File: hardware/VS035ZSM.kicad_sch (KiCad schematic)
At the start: 41 parts, among them IC3 TPS65131TRGERQ1, J2 FH35C-25S-0.3SHW_50_, J4 245863050104829+, U4 LP3320

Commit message: updated tps6513 footprint to vqfn24 + fixed some missing connections near it
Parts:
- IC3: footprint SamacSys_Parts:QFN50P400X400X100-25N-D -> Package_DFN_QFN:VQFN-24-1EP_4x4mm_P0.5mm_EP2.45x2.45mm
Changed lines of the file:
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@@
       (effects (font (size 1.27 1.27)))
     )
-    (property "Footprint" "SamacSys_Parts:QFN50P400X400X100-25N-D" (at 167.64 142.545 0)
+    (property "Footprint" "Package_DFN_QFN:VQFN-24-1EP_4x4mm_P0.5mm_EP2.45x2.45mm" (at 167.64 142.545 0)
       (effects (font (size 1.27 1.27)) (justify left top) hide)
     )

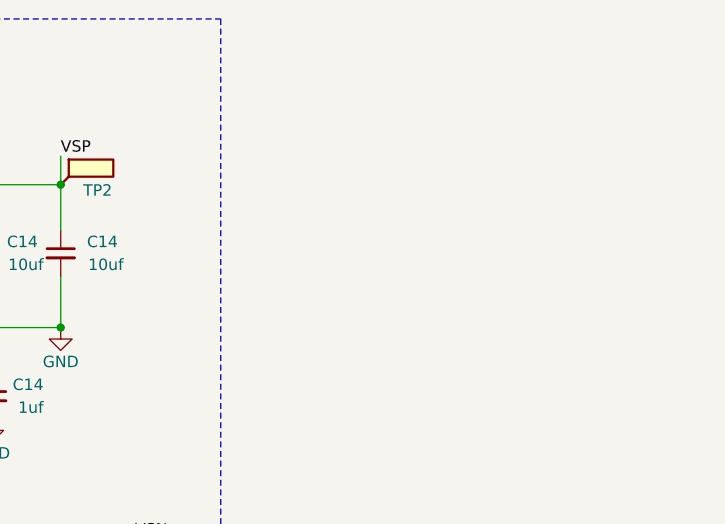
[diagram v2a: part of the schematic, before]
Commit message: added via stitching and updated the bias generator layout
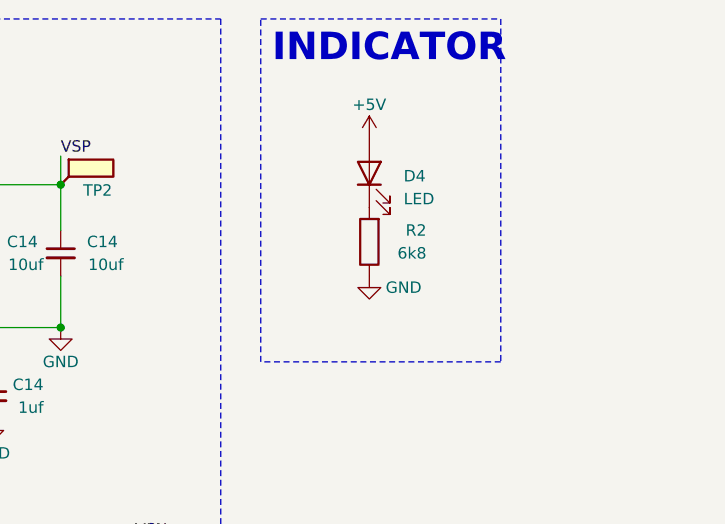
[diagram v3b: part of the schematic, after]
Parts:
- added D4: LED, LED_SMD:LED_0805_2012Metric, symbol Device:LED
- added R2: 6k8, Resistor_SMD:R_0603_1608Metric, symbol Device:R
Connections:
- net +5V: now also D4.2 (A)
- net GND: now also R2.1
- new net: D4.1 (K), R2.2
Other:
- note added: "INDICATOR"
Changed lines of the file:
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@@
+    (fill (type none))
+  )
+  (rectangle (start 227.33 14.605) (end 254 52.705)
+    (stroke (width 0) (type dash))
     (fill (type none))
   )
@@
     (effects (font (face "KiCad Font") (size 3.048 3.048) (thickness 0.3556) bold) (justify left bottom))
   )
+  (text "INDICATOR" (at 228.6 19.685 0)
+    (effects (font (face "KiCad Font") (size 3.048 3.048) (thickness 0.3556) bold) (justify left bottom))
+  )
   (text "DISP MEZZANINE" (at 17.145 93.345 0)
     (effects (font (face "KiCad Font") (size 3.048 3.048) (thickness 0.3556) bold) (justify left bottom))
@@
         (path "/e63e39d7-6ac0-4ffd-8aa3-1841a4541b55/aa1c650f-a854-42b3-a05e-cf0d26468eda"
           (reference "#PWR041") (unit 1)
+        )
+      )
+    )
+  )
+  (symbol (lib_id "Device:R") (at 239.395 39.37 180) (unit 1)
+    (in_bom yes) (on_board yes) (dnp no)
+    (property "Reference" "R2" (at 245.745 38.1 0)
+      (effects (font (size 1.27 1.27)) (justify left))
+    )
+    (property "Value" "6k8" (at 245.745 40.64 0)
+      (effects (font (size 1.27 1.27)) (justify left))
+    )
+    (property "Footprint" "Resistor_SMD:R_0603_1608Metric" (at 241.173 39.37 90)
+      (effects (font (size 1.27 1.27)) hide)
+    )
+    (property "Datasheet" "~" (at 239.395 39.37 0)
+      (effects (font (size 1.27 1.27)) hide)
+    )
+    (pin "1")
+    (pin "2")
+    (instances
+      (project "ssd2828_board"
+        (path "/e63e39d7-6ac0-4ffd-8aa3-1841a4541b55"
+          (reference "R2") (unit 1)
+        )
+        (path "/e63e39d7-6ac0-4ffd-8aa3-1841a4541b55/eadf4466-e824-4ab1-a46a-9025d68137a1"
+          (reference "R11") (unit 1)
+        )
+        (path "/e63e39d7-6ac0-4ffd-8aa3-1841a4541b55/d0befddb-c525-47aa-a36b-f999bfb6acb2"
+          (reference "R14") (unit 1)
+        )
+        (path "/e63e39d7-6ac0-4ffd-8aa3-1841a4541b55/aa1c650f-a854-42b3-a05e-cf0d26468eda"
+          (reference "R14") (unit 1)
         )
       )
@@
         (path "/e63e39d7-6ac0-4ffd-8aa3-1841a4541b55/aa1c650f-a854-42b3-a05e-cf0d26468eda"
           (reference "#PWR081") (unit 1)
+        )
+      )
+    )
+  )
+  (symbol (lib_name "GND_3") (lib_id "power:GND") (at 239.395 43.18 0) (unit 1)
+    (in_bom yes) (on_board yes) (dnp no)
+    (property "Reference" "#PWR03" (at 239.395 49.53 0)
+      (effects (font (size 1.27 1.27)) hide)
+    )
+    (property "Value" "GND" (at 243.205 44.45 0)
+      (effects (font (size 1.27 1.27)))
+    )
+    (property "Footprint" "" (at 239.395 43.18 0)
+      (effects (font (size 1.27 1.27)) hide)
+    )
+    (property "Datasheet" "" (at 239.395 43.18 0)
+      (effects (font (size 1.27 1.27)) hide)
+    )
+    (pin "1")
+    (instances
+      (project "ssd2828_board"
+        (path "/e63e39d7-6ac0-4ffd-8aa3-1841a4541b55"
+          (reference "#PWR03") (unit 1)
+        )
+        (path "/e63e39d7-6ac0-4ffd-8aa3-1841a4541b55/eadf4466-e824-4ab1-a46a-9025d68137a1"
+          (reference "#PWR099") (unit 1)
+        )
+        (path "/e63e39d7-6ac0-4ffd-8aa3-1841a4541b55/aa1c650f-a854-42b3-a05e-cf0d26468eda"
+          (reference "#PWR0101") (unit 1)
         )
       )
@@
     )
   )
+  (symbol (lib_id "Device:LED") (at 239.395 31.75 90) (unit 1)
+    (in_bom yes) (on_board yes) (dnp no) (fields_autoplaced)
+    (property "Reference" "D4" (at 243.205 32.0675 90)
+      (effects (font (size 1.27 1.27)) (justify right))
+    )
+    (property "Value" "LED" (at 243.205 34.6075 90)
+      (effects (font (size 1.27 1.27)) (justify right))
+    )
+    (property "Footprint" "LED_SMD:LED_0805_2012Metric" (at 239.395 31.75 0)
+      (effects (font (size 1.27 1.27)) hide)
+    )
+    (property "Datasheet" "~" (at 239.395 31.75 0)
+      (effects (font (size 1.27 1.27)) hide)
+    )
+    (pin "1")
+    (pin "2")
+    (instances
+      (project "ssd2828_board"
+        (path "/e63e39d7-6ac0-4ffd-8aa3-1841a4541b55/eadf4466-e824-4ab1-a46a-9025d68137a1"
+          (reference "D4") (unit 1)
+        )
+        (path "/e63e39d7-6ac0-4ffd-8aa3-1841a4541b55/aa1c650f-a854-42b3-a05e-cf0d26468eda"
+          (reference "D5") (unit 1)
+        )
+      )
+    )
+  )
   (symbol (lib_id "Device:C_Small") (at 205.105 40.64 0) (mirror y) (unit 1)
     (in_bom yes) (on_board yes) (dnp no)
@@
         )
       )
+    )
+  )
+  (symbol (lib_id "power:+5V") (at 239.395 27.94 0) (unit 1)
+    (in_bom yes) (on_board yes) (dnp no) (fields_autoplaced)
+    (property "Reference" "#PWR021" (at 239.395 31.75 0)
+      (effects (font (size 1.27 1.27)) hide)
+    )
+    (property "Value" "+5V" (at 239.395 24.13 0)
+      (effects (font (size 1.27 1.27)))
+    )
+    (property "Footprint" "" (at 239.395 27.94 0)
+      (effects (font (size 1.27 1.27)) hide)
+    )
+    (property "Datasheet" "" (at 239.395 27.94 0)
+      (effects (font (size 1.27 1.27)) hide)
+    )
+    (pin "1")
+    (instances
+      (project "ssd2828_board"
+        (path "/e63e39d7-6ac0-4ffd-8aa3-1841a4541b55/eadf4466-e824-4ab1-a46a-9025d68137a1"
+          (reference "#PWR021") (unit 1)
+        )
+        (path "/e63e39d7-6ac0-4ffd-8aa3-1841a4541b55/aa1c650f-a854-42b3-a05e-cf0d26468eda"
+          (reference "#PWR0100") (unit 1)
+        )
+      )

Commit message: fixed details
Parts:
- L5, L6: footprint Inductor_SMD:WPN252012 -> C98354:IND-SMD_L2.5-W2.0_WPN252012H
- L7: footprint Inductor_SMD:FHD252012 -> C602016:IND-SMD_L2.5-W2.0_FHD252012S-6R8MT
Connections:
- no-connect marks 0 -> 13
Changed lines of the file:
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@@
   (junction (at 27.94 140.335) (diameter 0) (color 0 0 0 0)
   )
+  (no_connect (at 67.945 112.395))
+  (no_connect (at 255.27 136.525))
+  (no_connect (at 67.945 120.015))
+  (no_connect (at 67.945 107.315))
+  (no_connect (at 67.945 125.095))
+  (no_connect (at 67.945 104.775))
+  (no_connect (at 252.73 136.525))
+  (no_connect (at 42.545 165.735))
+  (no_connect (at 67.945 122.555))
+  (no_connect (at 67.945 127.635))
+  (no_connect (at 250.19 136.525))
+  (no_connect (at 67.945 109.855))
+  (no_connect (at 42.545 160.655))
   (wire (pts (xy 83.185 130.175) (xy 83.185 132.715))
     (stroke (width 0) (type default))
@@
       (effects (font (size 1.27 1.27)))
     )
-    (property "Footprint" "Inductor_SMD:FHD252012" (at 135.89 123.19 0)
+    (property "Footprint" "C602016:IND-SMD_L2.5-W2.0_FHD252012S-6R8MT" (at 135.89 123.19 0)
       (effects (font (size 1.27 1.27)) hide)
     )
@@
       (effects (font (size 1.27 1.27)))
     )
-    (property "Footprint" "Inductor_SMD:WPN252012" (at 178.435 86.36 0)
+    (property "Footprint" "C98354:IND-SMD_L2.5-W2.0_WPN252012H" (at 178.435 86.36 0)
       (effects (font (size 1.27 1.27)) hide)
     )
@@
       (effects (font (size 1.27 1.27)))
     )
-    (property "Footprint" "Inductor_SMD:WPN252012" (at 132.08 33.02 0)
-      (effects (font (size 1.27 1.27)) hide)
-    )
+    (property "Footprint" "C98354:IND-SMD_L2.5-W2.0_WPN252012H" (at 132.08 33.02 0)
+      (effects (font (size 1.27 1.27)) hide)
+    )

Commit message: fixed some 3d models + redid power distribution on the BOE board
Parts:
- R2: footprint Resistor_SMD:R_0603_1608Metric -> Resistor_SMD:R_1210_3225Metric
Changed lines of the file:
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@@
       (effects (font (size 1.27 1.27)) (justify left))
     )
-    (property "Footprint" "Resistor_SMD:R_0603_1608Metric" (at 167.132 142.24 90)
+    (property "Footprint" "Resistor_SMD:R_1210_3225Metric" (at 167.132 142.24 90)
       (effects (font (size 1.27 1.27)) hide)
     )

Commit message: version 1.0
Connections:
- net +1V8: now also RN1.1 (R1.1)
- net GND: no longer RN1.1 (R1.1)
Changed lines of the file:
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@@
   (junction (at 195.58 90.17) (diameter 0) (color 0 0 0 0)
-  )
-  (junction (at 227.33 146.05) (diameter 0) (color 0 0 0 0)
   )
   (junction (at 178.435 90.17) (diameter 0) (color 0 0 0 0)
@@
     (stroke (width 0) (type default))
   )
+  (wire (pts (xy 220.345 147.955) (xy 224.79 147.955))
+    (stroke (width 0) (type default))
+  )
   (wire (pts (xy 178.435 76.2) (xy 178.435 71.755))
     (stroke (width 0) (type default))
@@
     (stroke (width 0) (type default))
   )
-  (wire (pts (xy 224.79 146.05) (xy 227.33 146.05))
-    (stroke (width 0) (type default))
-  )
   (wire (pts (xy 27.94 170.815) (xy 27.94 173.355))
     (stroke (width 0) (type default))
@@
     (stroke (width 0) (type default))
   )
+  (wire (pts (xy 224.79 147.955) (xy 224.79 146.05))
+    (stroke (width 0) (type default))
+  )
   (wire (pts (xy 34.925 107.315) (xy 42.545 107.315))
     (stroke (width 0) (type default))
@@
   )
   (wire (pts (xy 33.655 53.34) (xy 48.895 53.34))
+    (stroke (width 0) (type default))
+  )
+  (wire (pts (xy 220.345 146.05) (xy 220.345 147.955))
     (stroke (width 0) (type default))
   )
@@
         )
       )
+    )
+  )
+  (symbol (lib_id "power:+1V8") (at 220.345 146.05 0) (unit 1)
+    (in_bom yes) (on_board yes) (dnp no)
+    (property "Reference" "#PWR036" (at 220.345 149.86 0)
+      (effects (font (size 1.27 1.27)) hide)
+    )
+    (property "Value" "+1V8" (at 220.345 142.24 0)
+      (effects (font (size 1.27 1.27)))
+    )
+    (property "Footprint" "" (at 220.345 146.05 0)
+      (effects (font (size 1.27 1.27)) hide)
+    )
+    (property "Datasheet" "" (at 220.345 146.05 0)
+      (effects (font (size 1.27 1.27)) hide)
+    )
+    (pin "1")
+    (instances
+      (project "ssd2828_board"
+        (path "/e63e39d7-6ac0-4ffd-8aa3-1841a4541b55/eadf4466-e824-4ab1-a46a-9025d68137a1"
+          (reference "#PWR036") (unit 1)
+        )
+        (path "/e63e39d7-6ac0-4ffd-8aa3-1841a4541b55/d0befddb-c525-47aa-a36b-f999bfb6acb2"
+          (reference "#PWR046") (unit 1)
+        )
+        (path "/e63e39d7-6ac0-4ffd-8aa3-1841a4541b55/aa1c650f-a854-42b3-a05e-cf0d26468eda"
+          (reference "#PWR0105") (unit 1)
+        )
+      )

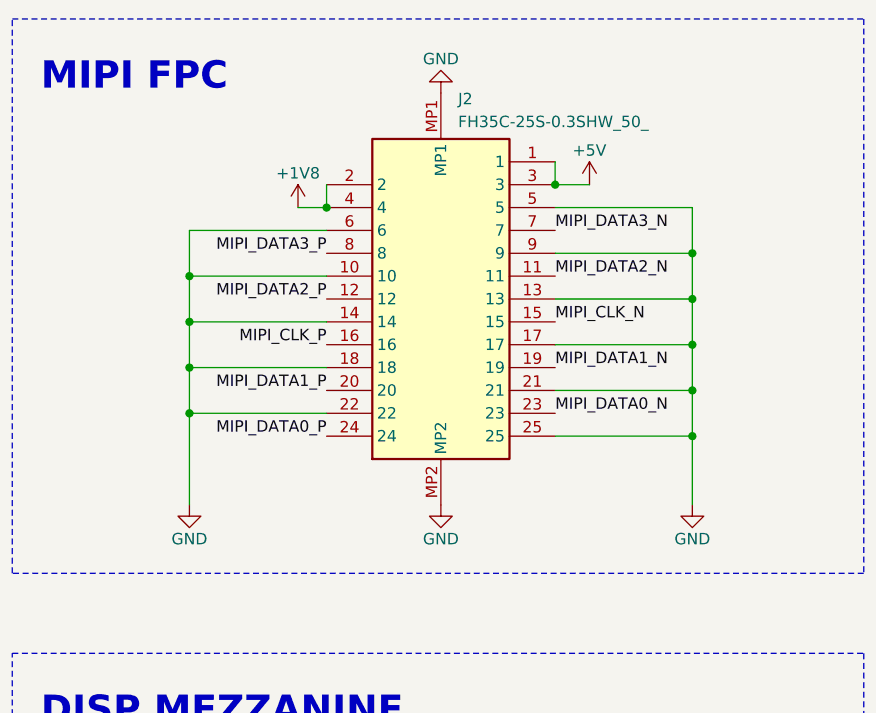
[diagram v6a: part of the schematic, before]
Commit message: fixed hirose FPC connector poinitng backwards on the 2 lcd boards+added stm32f401 boilerplate code
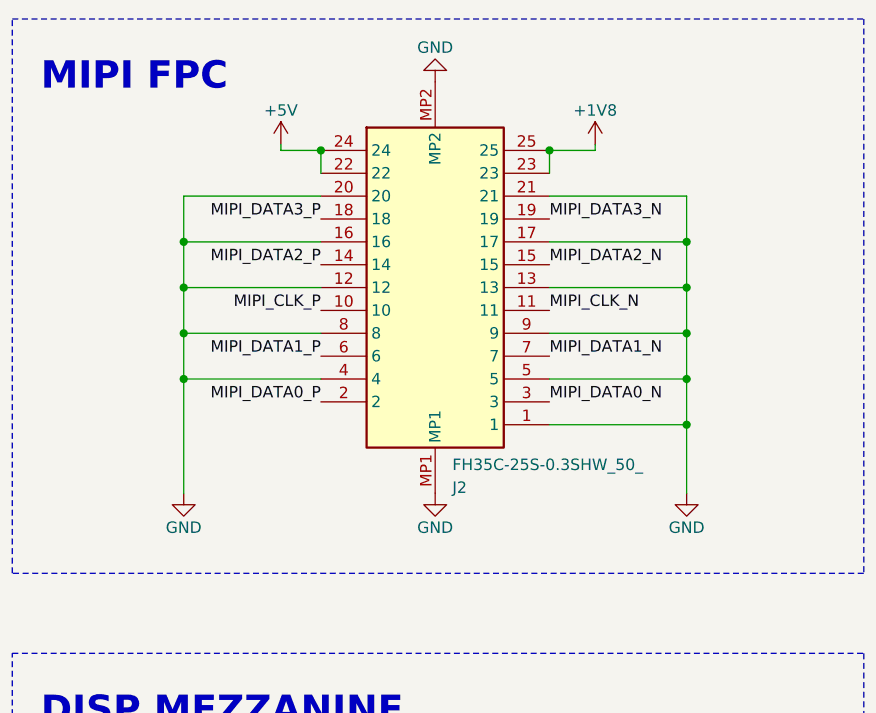
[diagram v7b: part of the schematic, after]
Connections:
- net +1V8: now also J2.23, J2.25; no longer J2.2, J2.4
- net +5V: now also J2.22, J2.24; no longer J2.1, J2.3
- net GND: now also J2.1, J2.12, J2.16, J2.20, J2.4, J2.8; no longer J2.10, J2.14, J2.18, J2.22, J2.25, J2.6
- net MIPI_CLK_N: now also J2.11; no longer J2.15
- net MIPI_CLK_P: now also J2.10; no longer J2.16
- net MIPI_DATA0_N: now also J2.3; no longer J2.23
- net MIPI_DATA0_P: now also J2.2; no longer J2.24
- net MIPI_DATA1_N: now also J2.7; no longer J2.19
- net MIPI_DATA1_P: now also J2.6; no longer J2.20
- net MIPI_DATA2_N: now also J2.15; no longer J2.11
- net MIPI_DATA2_P: now also J2.14; no longer J2.12
- net MIPI_DATA3_N: now also J2.19; no longer J2.7
- net MIPI_DATA3_P: now also J2.18; no longer J2.8
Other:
- moved on the sheet: J2
